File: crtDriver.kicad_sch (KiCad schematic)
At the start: 9 parts

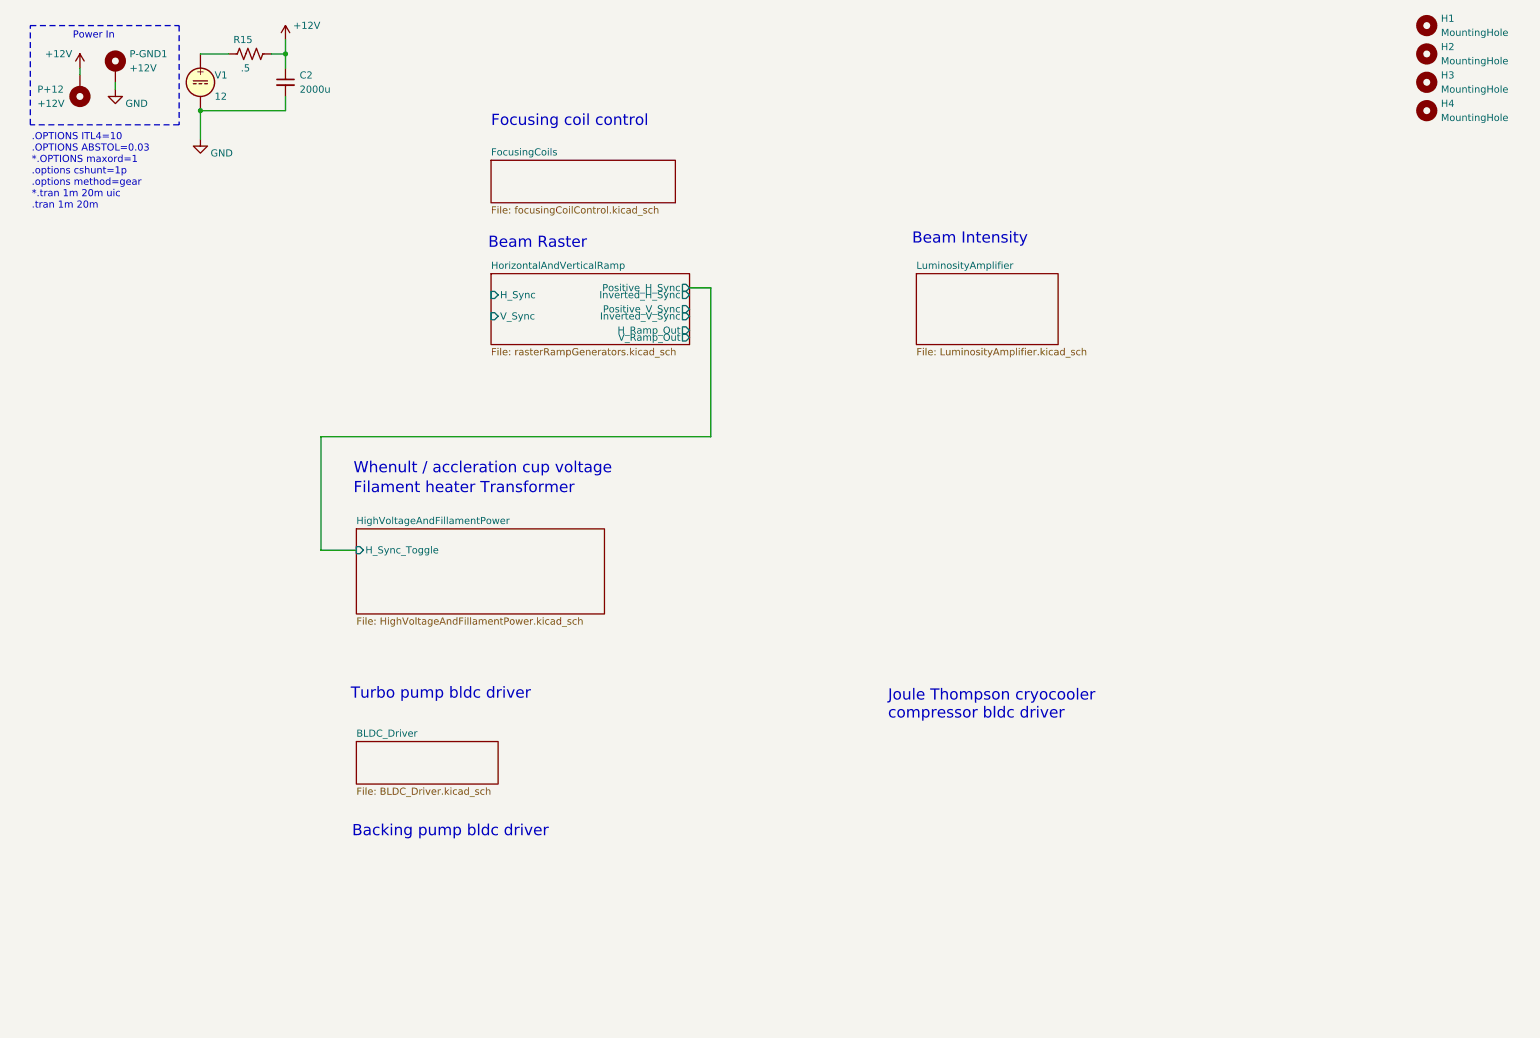
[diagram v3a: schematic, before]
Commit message: added new spice directives to improve simulation speed, added sections for motor drivers, micro controlers, i2c bus connections, realized that focusing coils, hv, horizontal and vertical ramp will need time stable signals (not voltage dependant like with a voltage controlled oscilator) so it will be much simpler to design them with micro controllers
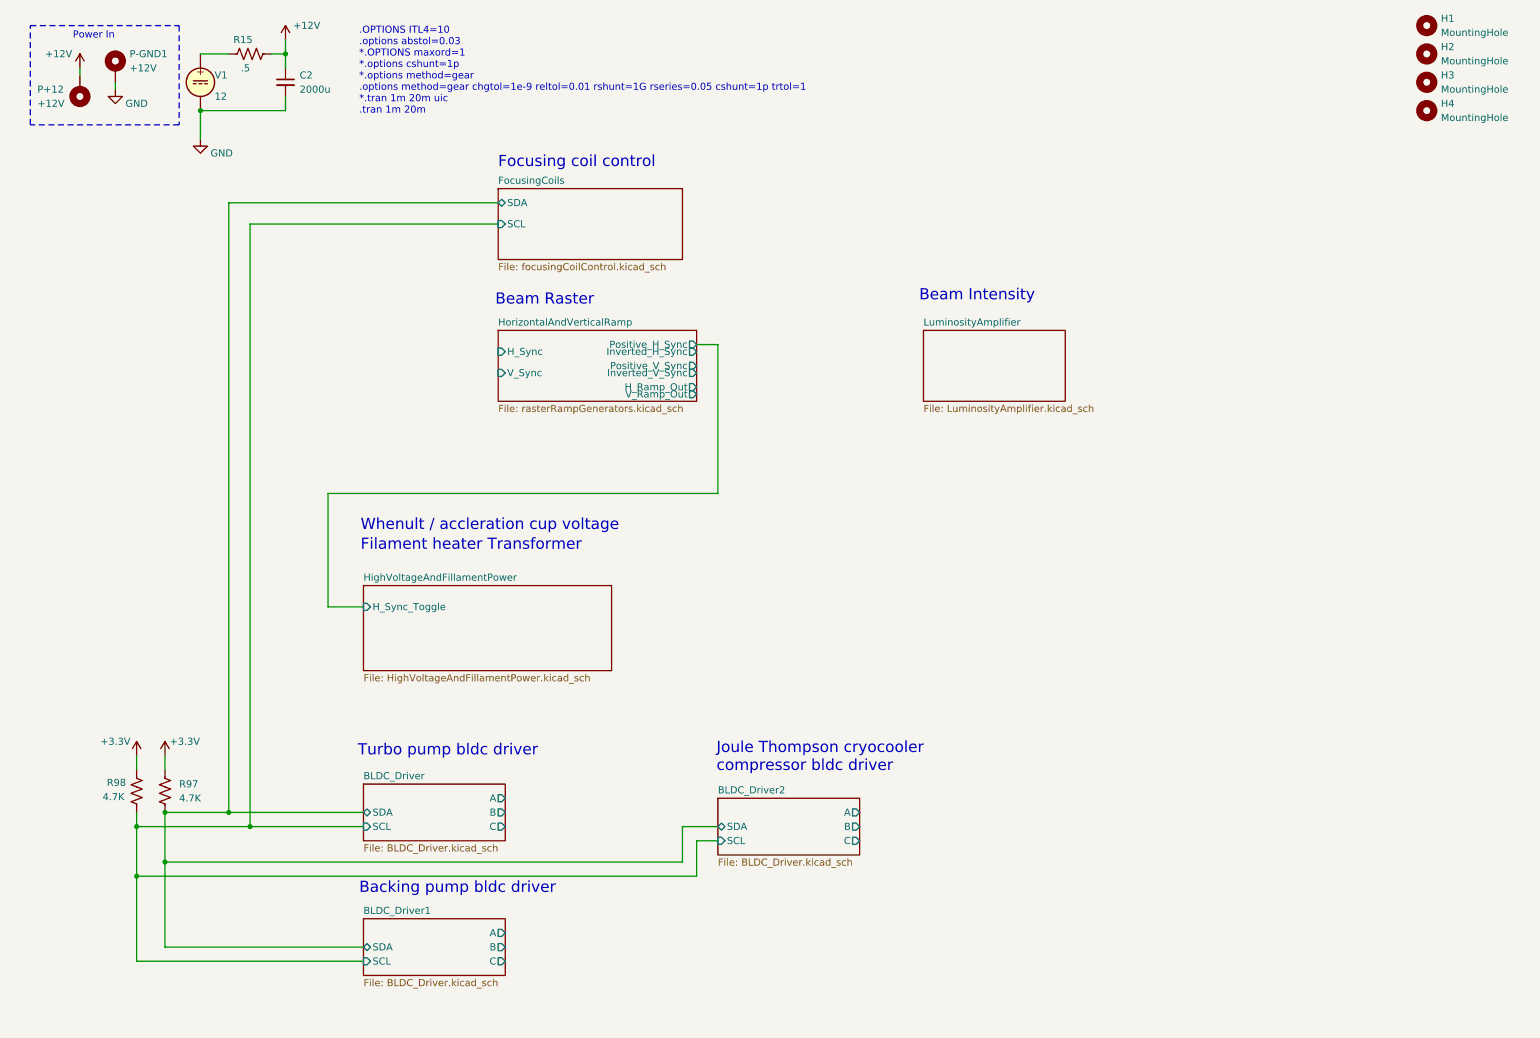
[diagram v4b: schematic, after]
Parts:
- added R97, R98: 4.7K, symbol Device:R_US
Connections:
- new net +3.3V: R97.1, R98.1
- new net BLDC_Driver/SCL: R98.2
- new net BLDC_Driver/SDA: R97.2
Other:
- added sheet BLDC_Driver1 (BLDC_Driver.kicad_sch)
- added sheet BLDC_Driver2 (BLDC_Driver.kicad_sch)
- sheet BLDC_Driver ports: added A, B, C, SCL, SDA; removed none
- sheet FocusingCoils ports: added SCL, SDA; removed none
- note added: ".OPTIONS ITL4=10 .options abstol=0.03 *.OPTIONS maxord=1 *.options cshunt=1p *.options method=gear .options method=gear chgtol=1e-9 reltol=0.01 rshunt=1G rseries=0.05 cshunt=1p trtol=1 *.tran 1m 20m uic .tran 1m 20m"
- note removed: ".OPTIONS ITL4=10 .OPTIONS ABSTOL=0.03 *.OPTIONS maxord=1 .options cshunt=1p .options method=gear *.tran 1m 20m uic .tran 1m 20m"

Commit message: changed bldc driver schematic to use esp32 devkit
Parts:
- R97, R98: footprint (none) -> Resistor_SMD:R_0603_1608Metric
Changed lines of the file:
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@@
 			)
 		)
-		(property "Footprint" ""
+		(property "Footprint" "Resistor_SMD:R_0603_1608Metric"
 			(at 41.656 153.924 90)
 			(effects
@@
 			)
 		)
-		(property "Footprint" ""
+		(property "Footprint" "Resistor_SMD:R_0603_1608Metric"
 			(at 36.576 153.924 90)
 			(effects

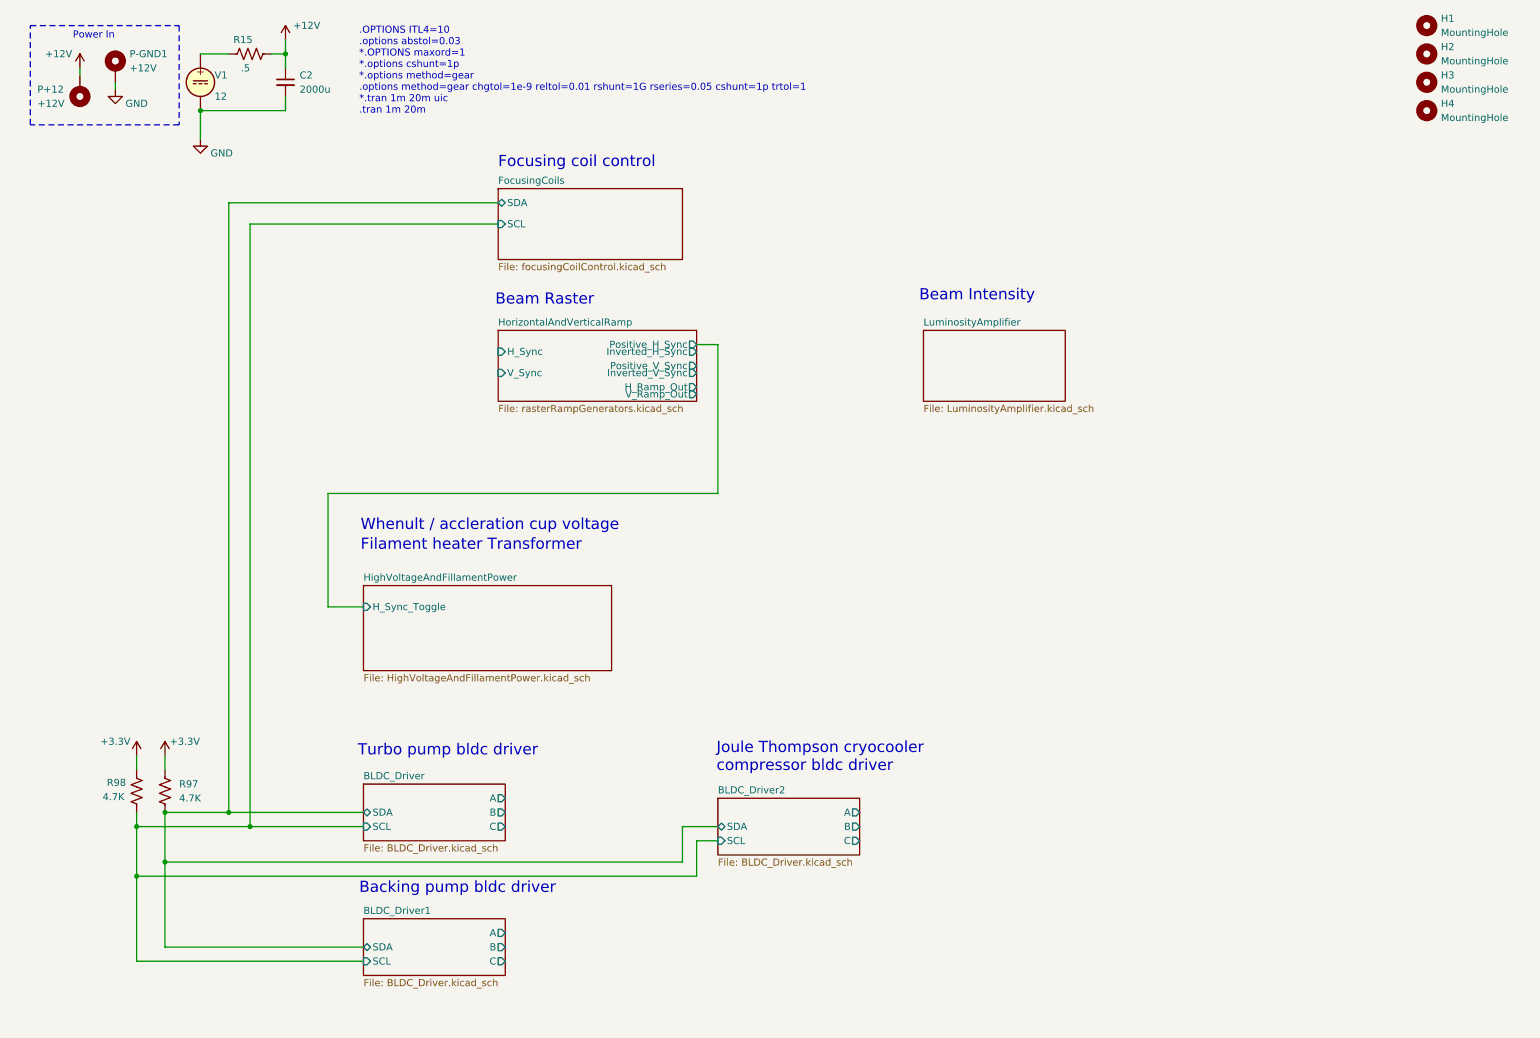
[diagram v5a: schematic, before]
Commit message: added sections to add to overview schematic, added some of the component schematics
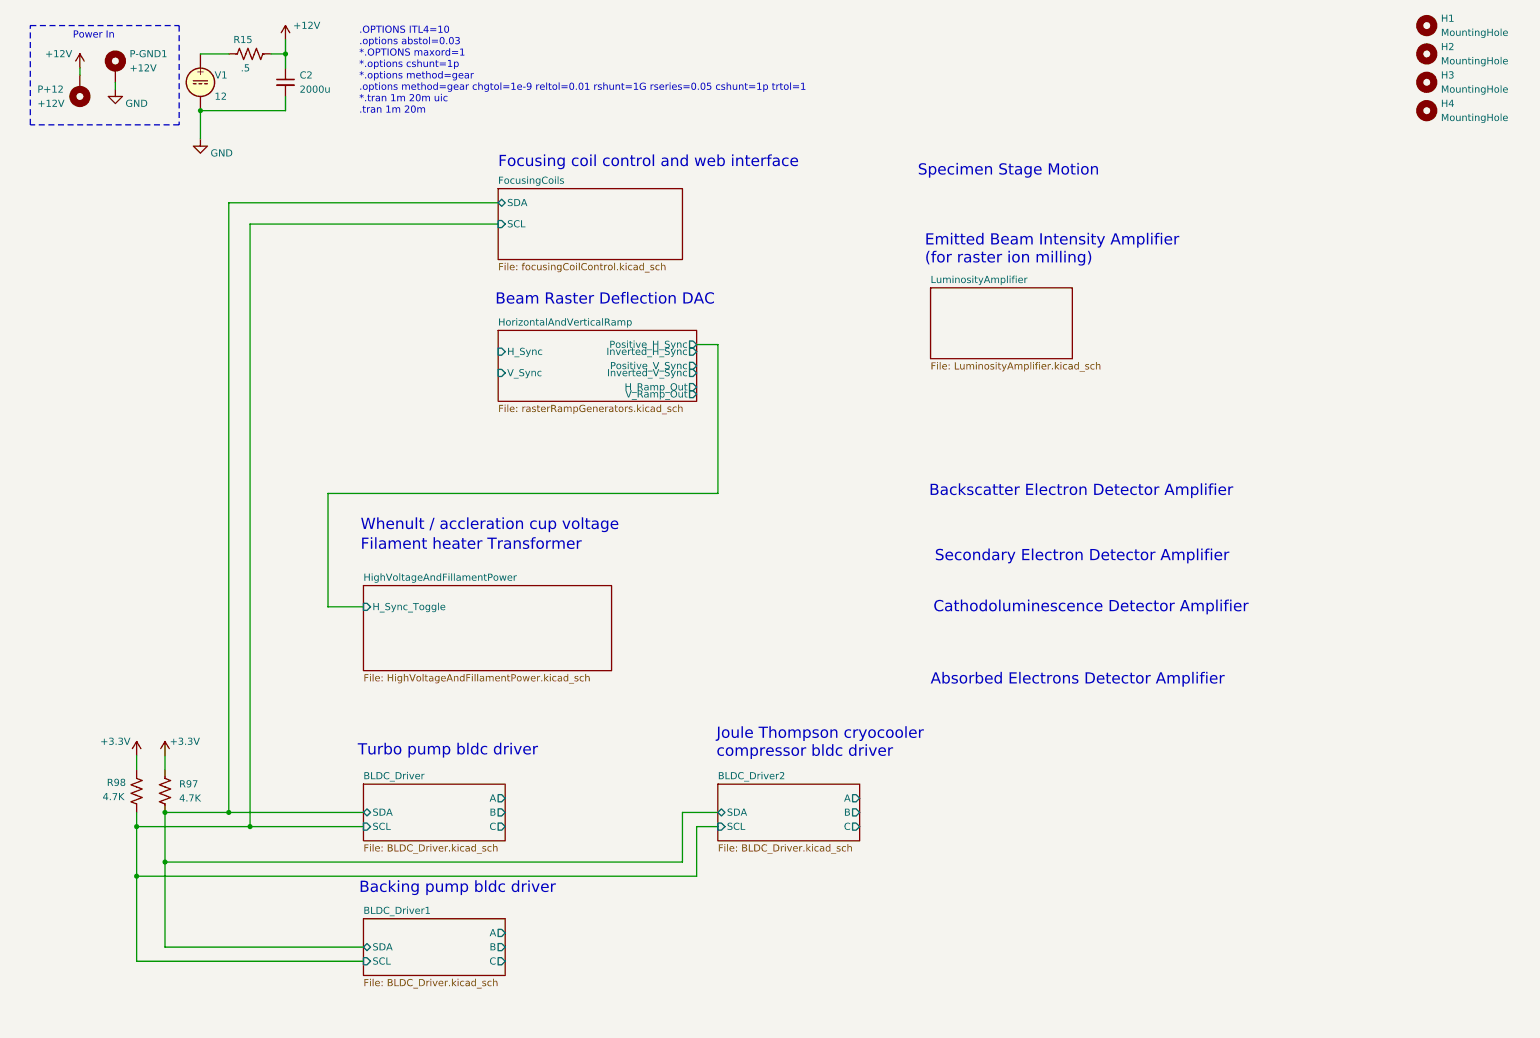
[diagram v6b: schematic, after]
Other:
- note added: "Absorbed Electrons Detector Amplifier"
- note added: "Backscatter Electron Detector Amplifier"
- note added: "Beam Raster Deflection DAC"
- note added: "Cathodoluminescence Detector Amplifier"
- note added: "Emitted Beam Intensity Amplifier (for raster ion milling)"
- note added: "Focusing coil control and web interface"
- note added: "Secondary Electron Detector Amplifier"
- note added: "Specimen Stage Motion"
- note removed: "Beam Intensity"
- note removed: "Beam Raster"
- note removed: "Focusing coil control"
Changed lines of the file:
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@@
 	(wire
 		(pts
-			(xy 135.89 162.56) (xy 139.7 162.56)
+			(xy 135.89 160.02) (xy 139.7 160.02)
 		)
 		(stroke
@@
 	(wire
 		(pts
-			(xy 139.7 160.02) (xy 133.35 160.02)
+			(xy 139.7 157.48) (xy 133.35 157.48)
 		)
 		(stroke
@@
 	(wire
 		(pts
-			(xy 135.89 162.56) (xy 135.89 168.91)
+			(xy 135.89 160.02) (xy 135.89 168.91)
 		)
 		(stroke
@@
 	(wire
 		(pts
-			(xy 133.35 160.02) (xy 133.35 166.37)
+			(xy 133.35 157.48) (xy 133.35 166.37)
 		)
 		(stroke
@@
 		)
 	)
+	(text "Secondary Electron Detector Amplifier"
+		(exclude_from_sim no)
+		(at 178.562 112.776 0)
+		(effects
+			(font
+				(size 2 2)
+			)
+			(justify left bottom)
+		)
+	)
 	(text "Joule Thompson cryocooler\ncompressor bldc driver"
 		(exclude_from_sim no)
-		(at 139.446 150.368 0)
+		(at 139.446 147.828 0)
 		(effects
 			(font
@@
 		)
 	)
+	(text "Specimen Stage Motion"
+		(exclude_from_sim no)
+		(at 175.514 43.688 0)
+		(effects
+			(font
+				(size 2 2)
+			)
+			(justify left bottom)
+		)
+	)
 	(text "Whenult / accleration cup voltage"
 		(exclude_from_sim no)
@@
 		)
 	)
+	(text "Cathodoluminescence Detector Amplifier"
+		(exclude_from_sim no)
+		(at 178.308 121.92 0)
+		(effects
+			(font
+				(size 2 2)
+			)
+			(justify left bottom)
+		)
+	)
 	(text ".OPTIONS ITL4=10\n.options abstol=0.03\n*.OPTIONS maxord=1\n*.options cshunt=1p\n*.options method=gear\n.options method=gear chgtol=1e-9 reltol=0.01 rshunt=1G rseries=0.05 cshunt=1p trtol=1\n*.tran 1m 20m uic\n.tran 1m 20m"
 		(exclude_from_sim no)
@@
 		)
 	)
-	(text "Beam Intensity"
-		(exclude_from_sim no)
-		(at 175.768 66.04 0)
+	(text "Backscatter Electron Detector Amplifier"
+		(exclude_from_sim no)
+		(at 177.546 101.092 0)
 		(effects
 			(font
@@
 		)
 	)
-	(text "Beam Raster"
+	(text "Emitted Beam Intensity Amplifier\n(for raster ion milling)"
+		(exclude_from_sim no)
+		(at 176.784 59.436 0)
+		(effects
+			(font
+				(size 2 2)
+			)
+			(justify left bottom)
+		)
+	)
+	(text "Beam Raster Deflection DAC"
 		(exclude_from_sim no)
 		(at 99.822 66.802 0)
@@
 		)
 	)
-	(text "Focusing coil control"
+	(text "Focusing coil control and web interface"
 		(exclude_from_sim no)
 		(at 100.33 42.164 0)
+		(effects
+			(font
+				(size 2 2)
+			)
+			(justify left bottom)
+		)
+	)
+	(text "Absorbed Electrons Detector Amplifier"
+		(exclude_from_sim no)
+		(at 177.8 134.874 0)
 		(effects
 			(font
@@
 	)
 	(sheet
-		(at 139.7 154.94)
+		(at 139.7 152.4)
 		(size 25.4 10.16)
 		(fields_autoplaced yes)
@@
 		)
 		(property "Sheetname" "BLDC_Driver2"
-			(at 139.7 154.2284 0)
+			(at 139.7 151.6884 0)
 			(effects
 				(font
@@
 		)
 		(property "Sheetfile" "BLDC_Driver.kicad_sch"
-			(at 139.7 165.6846 0)
+			(at 139.7 163.1446 0)
 			(effects
 				(font
@@
 		)
 		(pin "SDA" bidirectional
+			(at 139.7 157.48 180)
+			(effects
+				(font
+					(size 1.27 1.27)
+				)
+				(justify left)
+			)
+		)
+		(pin "SCL" input
 			(at 139.7 160.02 180)
 			(effects
@@
 			)
 		)
-		(pin "SCL" input
-			(at 139.7 162.56 180)
-			(effects
-				(font
-					(size 1.27 1.27)
-				)
-				(justify left)
-			)
-		)
 		(pin "B" output
+			(at 165.1 157.48 0)
+			(effects
+				(font
+					(size 1.27 1.27)
+				)
+				(justify right)
+			)
+		)
+		(pin "A" output
+			(at 165.1 154.94 0)
+			(effects
+				(font
+					(size 1.27 1.27)
+				)
+				(justify right)
+			)
+		)
+		(pin "C" output
 			(at 165.1 160.02 0)
-			(effects
-				(font
-					(size 1.27 1.27)
-				)
-				(justify right)
-			)
-		)
-		(pin "A" output
-			(at 165.1 157.48 0)
-			(effects
-				(font
-					(size 1.27 1.27)
-				)
-				(justify right)
-			)
-		)
-		(pin "C" output
-			(at 165.1 162.56 0)
 			(effects
 				(font
@@
 	)
 	(sheet
-		(at 176.53 71.12)
+		(at 177.8 63.5)
 		(size 25.4 12.7)
 		(fields_autoplaced yes)
@@
 		)
 		(property "Sheetname" "LuminosityAmplifier"
-			(at 176.53 70.4084 0)
+			(at 177.8 62.7884 0)
 			(effects
 				(font
@@
 		)
 		(property "Sheetfile" "LuminosityAmplifier.kicad_sch"
-			(at 176.53 84.4046 0)
-			(effects
-				(font
+			(at 177.8 76.7846 0)
+			(effects
+				(font
